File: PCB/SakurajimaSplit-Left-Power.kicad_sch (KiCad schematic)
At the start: 17 parts, among them J3 USB_C_Receptacle_USB2.0_16P, U2 TLV76733DRVx, U3 USBLC6-2SC6

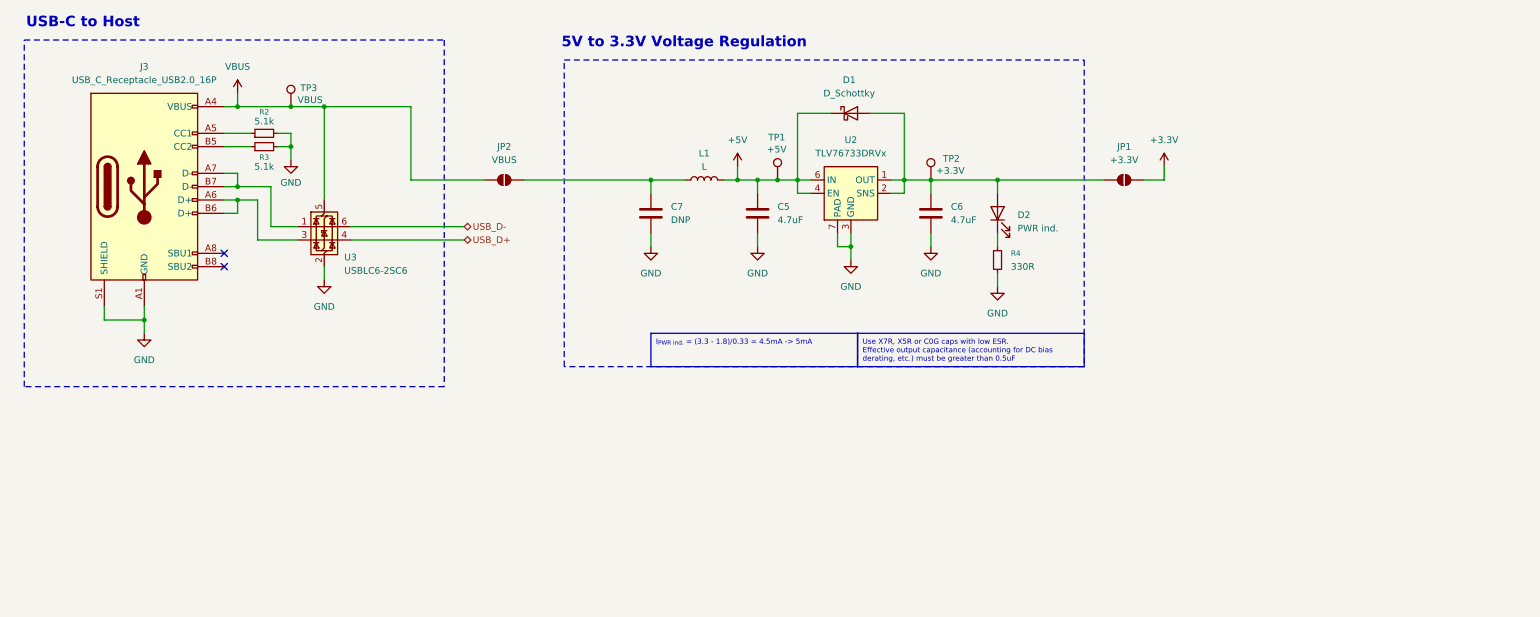
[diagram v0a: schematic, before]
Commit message: feat(sch): add USB to right-half circuit
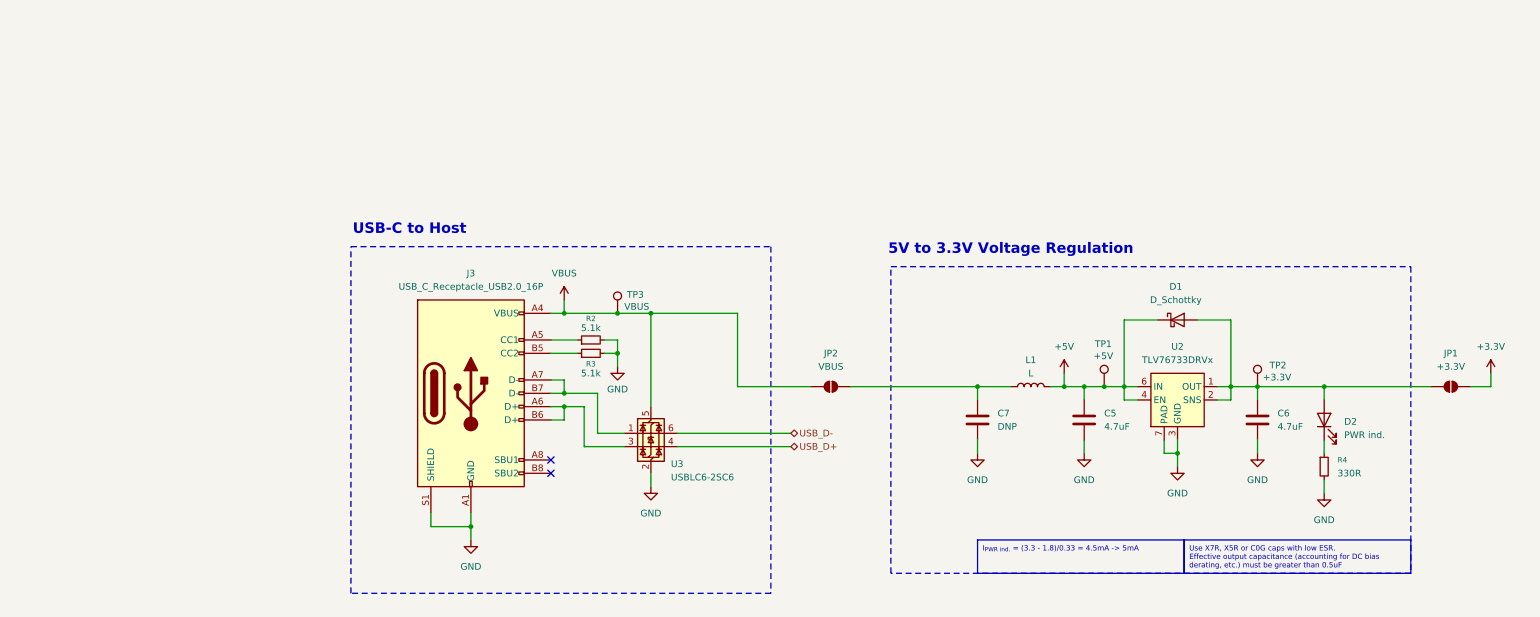
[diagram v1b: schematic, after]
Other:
- moved on the sheet: C5, C6, C7, D1, D2, J3, JP1, JP2, L1, R2, R3, R4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

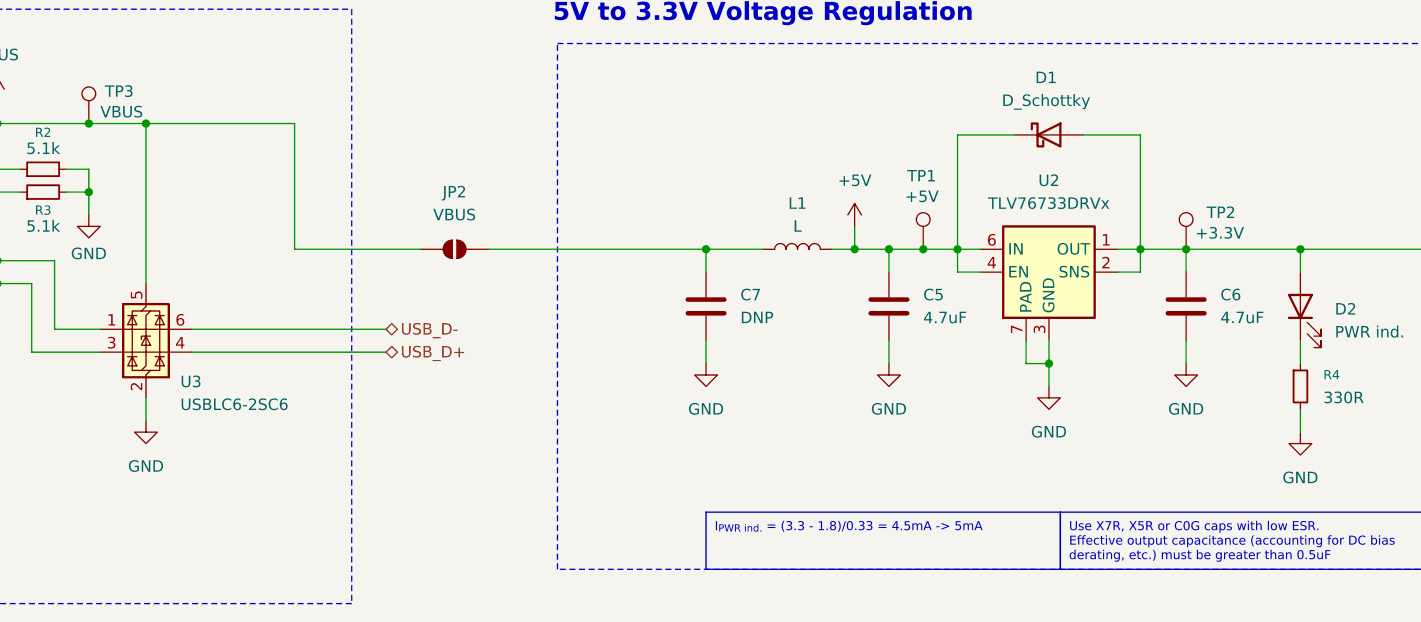
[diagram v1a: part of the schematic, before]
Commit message: feat(sch): mcu connections, test points and schematic cleanup
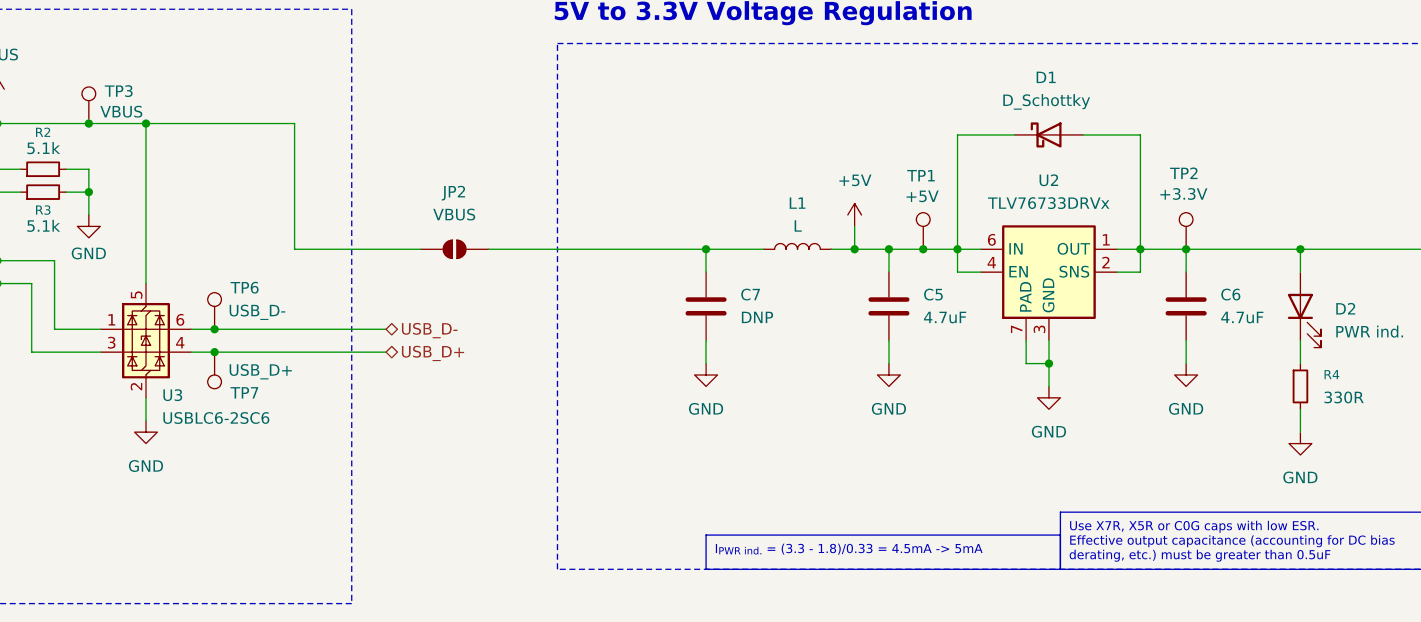
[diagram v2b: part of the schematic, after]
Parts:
- added TP6: USB_D-, symbol Connector:TestPoint
- added TP7: USB_D+, symbol Connector:TestPoint
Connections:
- net USB_D+: now also TP7.1
- net USB_D-: now also TP6.1
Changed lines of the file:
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@@
 	(text_box "I_{PWR ind.} = (3.3 - 1.8)/0.33 = 4.5mA -> 5mA"
 		(exclude_from_sim no)
-		(at 226.06 160.02 0)
-		(size 39.37 6.35)
+		(at 226.06 162.56 0)
+		(size 39.37 3.81)
 		(margins 0.9525 0.9525 0.9525 0.9525)
 		(stroke
@@
 	)
 	(junction
+		(at 171.45 142.24)
+		(diameter 0)
+		(color 0 0 0 0)
+	)
+	(junction
 		(at 246.38 130.81)
 		(diameter 0)
@@
 	)
 	(junction
+		(at 171.45 139.7)
+		(diameter 0)
+		(color 0 0 0 0)
+	)
+	(junction
 		(at 264.16 143.51)
 		(diameter 0)
@@
 	(wire
 		(pts
+			(xy 171.45 142.24) (xy 168.91 142.24)
+		)
+		(stroke
+			(width 0)
+			(type default)
+		)
+	)
+	(wire
+		(pts
 			(xy 246.38 140.97) (xy 246.38 143.51)
 		)
@@
 	(wire
 		(pts
-			(xy 190.5 139.7) (xy 168.91 139.7)
+			(xy 190.5 139.7) (xy 171.45 139.7)
 		)
 		(stroke
@@
 	(wire
 		(pts
-			(xy 190.5 142.24) (xy 168.91 142.24)
+			(xy 190.5 142.24) (xy 171.45 142.24)
 		)
 		(stroke
@@
 		(pts
 			(xy 157.48 116.84) (xy 163.83 116.84)
+		)
+		(stroke
+			(width 0)
+			(type default)
+		)
+	)
+	(wire
+		(pts
+			(xy 171.45 139.7) (xy 168.91 139.7)
 		)
 		(stroke
@@
 		(dnp no)
 		(property "Reference" "TP2"
-			(at 281.686 126.746 0)
+			(at 277.622 122.428 0)
 			(effects
 				(font
@@
 		)
 		(property "Value" "+3.3V"
-			(at 280.416 129.032 0)
+			(at 276.352 124.714 0)
 			(effects
 				(font
@@
 		(dnp no)
 		(property "Reference" "U3"
-			(at 167.64 145.542 0)
+			(at 165.608 147.066 0)
 			(effects
 				(font
@@
 		)
 		(property "Value" "USBLC6-2SC6"
-			(at 167.64 148.082 0)
+			(at 165.608 149.606 0)
 			(effects
 				(font
@@
 	)
 	(symbol
+		(lib_id "Connector:TestPoint")
+		(at 171.45 139.7 0)
+		(unit 1)
+		(exclude_from_sim no)
+		(in_bom yes)
+		(on_board yes)
+		(dnp no)
+		(property "Reference" "TP6"
+			(at 173.228 135.128 0)
+			(effects
+				(font
+					(size 1.27 1.27)
+				)
+				(justify left)
+			)
+		)
+		(property "Value" "USB_D-"
+			(at 172.974 137.668 0)
+			(effects
+				(font
+					(size 1.27 1.27)
+				)
+				(justify left)
+			)
+		)
+		(property "Footprint" ""
+			(at 176.53 139.7 0)
+			(effects
+				(font
+					(size 1.27 1.27)
+				)
+				(hide yes)
+			)
+		)
+		(property "Datasheet" "~"
+			(at 176.53 139.7 0)
+			(effects
+				(font
+					(size 1.27 1.27)
+				)
+				(hide yes)
+			)
+		)
+		(property "Description" "test point"
+			(at 171.45 139.7 0)
+			(effects
+				(font
+					(size 1.27 1.27)
+				)
+				(hide yes)
+			)
+		)
+		(pin "1"
+		)
+		(instances
+			(project "SakurajimaSplit"
+				(path "/2049b6de-7453-46e1-ab60-70116abff9d6/d08add9a-e5d5-49be-809e-a90adb11436d/38f7f4db-d52f-4e97-96ce-fcb5b455730e"
+					(reference "TP6")
+					(unit 1)
+				)
+			)
+		)
+	)
+	(symbol
 		(lib_id "power:GND")
 		(at 163.83 149.86 0)
@@
 					(unit 1)
 				)
+			)
+		)
+	)
+	(symbol
+		(lib_id "Connector:TestPoint")
+		(at 171.45 142.24 0)
+		(mirror x)
+		(unit 1)
+		(exclude_from_sim no)
+		(in_bom yes)
+		(on_board yes)
+		(dnp no)
+		(property "Reference" "TP7"
+			(at 173.228 146.812 0)
+			(effects
+				(font
+					(size 1.27 1.27)
+				)
+				(justify left)
+			)
+		)
+		(property "Value" "USB_D+"
+			(at 172.974 144.272 0)
+			(effects
+				(font
+					(size 1.27 1.27)
+				)
+				(justify left)
+			)
+		)
+		(property "Footprint" ""
+			(at 176.53 142.24 0)
+			(effects
+				(font
+					(size 1.27 1.27)
+				)
+				(hide yes)
+			)
+		)
+		(property "Datasheet" "~"
+			(at 176.53 142.24 0)
+			(effects
+				(font
+					(size 1.27 1.27)
+				)
+				(hide yes)
+			)
+		)
+		(property "Description" "test point"
+			(at 171.45 142.24 0)
+			(effects
+				(font
+					(size 1.27 1.27)
+				)
+				(hide yes)
+			)
+		)
+		(pin "1"
+		)
+		(instances
+			(project "SakurajimaSplit"
+				(path "/2049b6de-7453-46e1-ab60-70116abff9d6/d08add9a-e5d5-49be-809e-a90adb11436d/38f7f4db-d52f-4e97-96ce-fcb5b455730e"
+					(reference "TP7")
+					(unit 1)
+				)

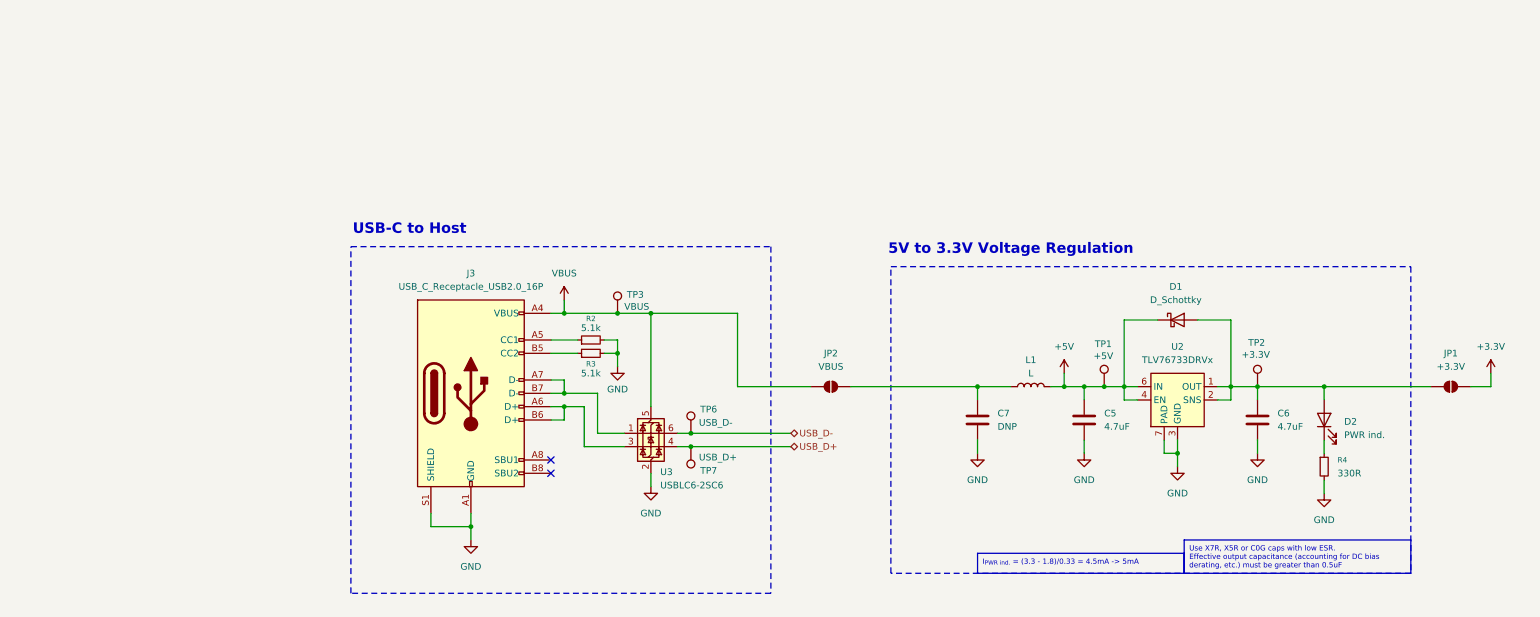
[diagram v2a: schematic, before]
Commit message: feat(sch): cleanup and anotate schematic, choose components
- Fixed mistakes in schematic
- Anotated the schematic
- Found and chose components
- Added GND test points
- Ran ERC and fixed all errors and warnings
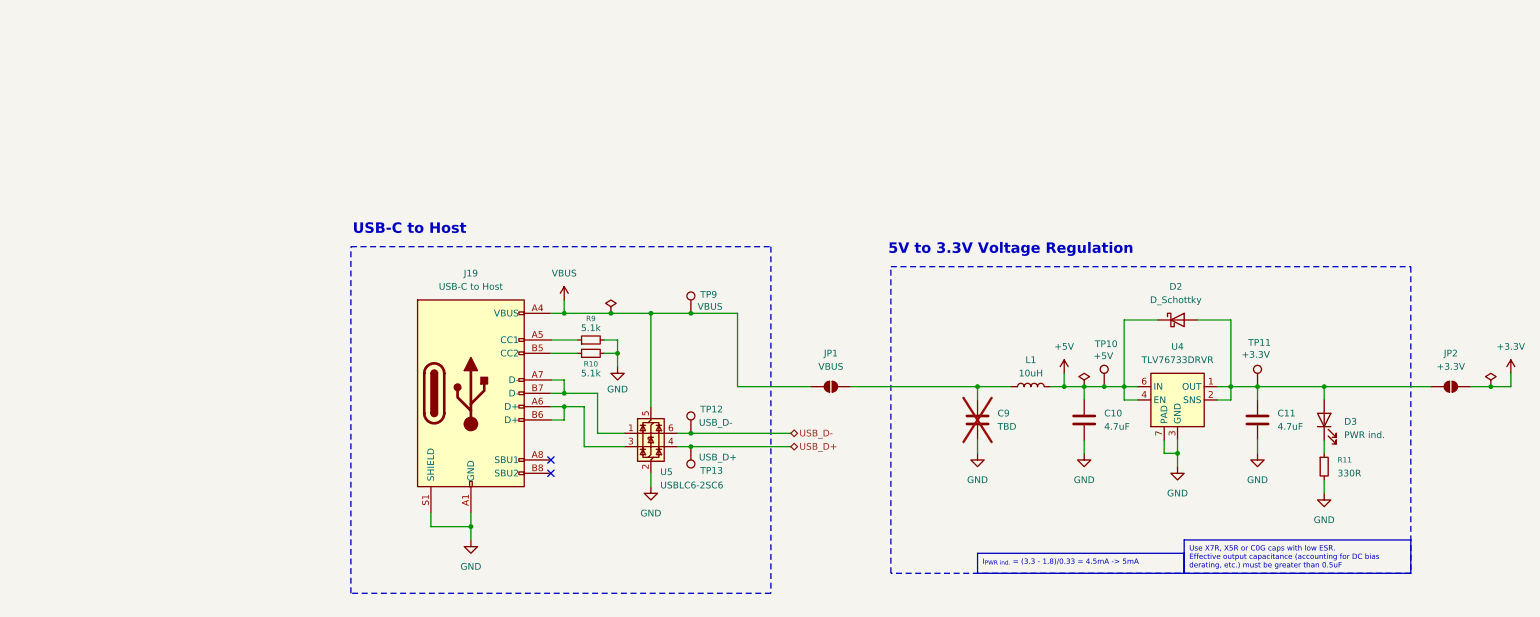
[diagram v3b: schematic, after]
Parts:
- removed J3: USB_C_Receptacle_USB2.0_16P, symbol Connector:USB_C_Receptacle_USB2.0_16P
- added J19: USB-C to Host, symbol Connector:USB_C_Receptacle_USB2.0_16P
- C10: renamed from C5; Distributor Link (none) -> https://lionelectronic.ir/products/4714-GRM21BR61H475KE51L; Manufacturer (none) -> Murata; Manufacturer Part No. (none) -> GRM21BR61H475KE51L
- C11: renamed from C6; Distributor Link (none) -> https://lionelectronic.ir/products/4714-GRM21BR61H475KE51L; Manufacturer (none) -> Murata; Manufacturer Part No. (none) -> GRM21BR61H475KE51L
- C9: renamed from C7; value DNP -> TBD; Distributor Link (none) -> https://lionelectronic.ir/products/4714-GRM21BR61H475KE51L; Manufacturer (none) -> Murata; Manufacturer Part No. (none) -> GRM21BR61H475KE51L; now not fitted
- D2: renamed from D1; Distributor Link (none) -> https://lionelectronic.ir/products/5692-B0530W-7-F; Manufacturer (none) -> Diodes Incorporated; Manufacturer Part No. (none) -> B0530W-7-F
- D3: renamed from D2; Distributor Link (none) -> https://lionelectronic.ir/products/2212-XL-1608UGC-04; Manufacturer (none) -> XINGLIGHT; Manufacturer Part No. (none) -> XL-1608UGC-04
- L1: value L -> 10uH; Distributor Link (none) -> https://lionelectronic.ir/products/4794-DFE322512F-100M%3DP2; Manufacturer (none) -> Murata; Manufacturer Part No. (none) -> DFE322512F-100M
- R10: renamed from R3; Distributor Link (none) -> https://lionelectronic.ir/products/1212-0603WAF5101T5E; Manufacturer (none) -> UniOhm; Manufacturer Part No. (none) -> 0603WAF5101T5E
- R11: renamed from R4; Distributor Link (none) -> https://lionelectronic.ir/products/1182-SER0603F330R; Manufacturer (none) -> VO Sub Brand (ER); Manufacturer Part No. (none) -> SER0603F330R
- R9: renamed from R2; Distributor Link (none) -> https://lionelectronic.ir/products/1212-0603WAF5101T5E; Manufacturer (none) -> UniOhm; Manufacturer Part No. (none) -> 0603WAF5101T5E
- TP10: renamed from TP1; now left out of the parts list
- TP11: renamed from TP2; now left out of the parts list
- TP12: renamed from TP6; now left out of the parts list
- TP13: renamed from TP7; now left out of the parts list
- TP9: renamed from TP3; now left out of the parts list
- U4: renamed from U2; value TLV76733DRVx -> TLV76733DRVR; Distributor Link (none) -> https://lionelectronic.ir/products/4877-TLV76733DRVR; Manufacturer (none) -> Texas Instruments; Manufacturer Part No. (none) -> TLV76733DRVR
- U5: renamed from U3; Distributor Link (none) -> https://lionelectronic.ir/products/4780-USBLC6-4SC6; Manufacturer (none) -> STMicroelectronics; Manufacturer Part No. (none) -> USBLC6-4SC6
- renumbered JP2 to JP1, JP1 to JP2
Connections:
- net GND: now also J19.A1 (GND), J19.A12 (GND), J19.B1 (GND), J19.B12 (GND), J19.S1 (SHIELD)
- net VBUS: now also J19.A4 (VBUS), J19.A9 (VBUS), J19.B4 (VBUS), J19.B9 (VBUS)
- net at R10.1: now also J19.B5 (CC2)
- net at U5.1 (I/O1): now also J19.A7 (D-), J19.B7 (D-)
- net at U5.3 (I/O2): now also J19.A6 (D+), J19.B6 (D+)
- net at R9.1: now also J19.A5 (CC1)
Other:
- moved on the sheet: TP9

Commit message: feat(sch): design right half of the keyboard
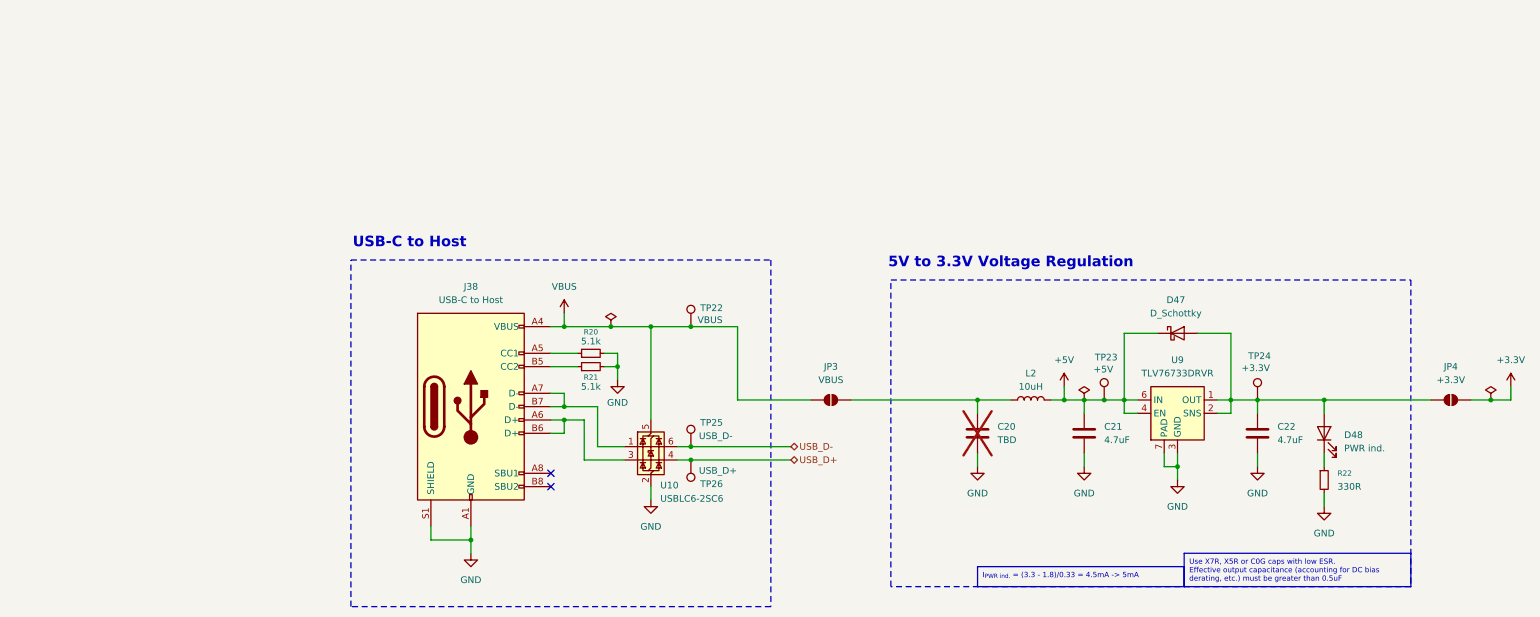
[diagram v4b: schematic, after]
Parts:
- renumbered C9 to C20, C10 to C21, C11 to C22, D2 to D47, D3 to D48, J19 to J38, JP1 to JP3, JP2 to JP4, L1 to L2, R9 to R20, R10 to R21, R11 to R22, TP9 to TP22, TP10 to TP23, TP11 to TP24, TP12 to TP25, TP13 to TP26, U5 to U10, U4 to U9
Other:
- moved on the sheet: C20, C21, C22, D47, D48, J38, JP3, JP4, L2, R20, R21, R22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
